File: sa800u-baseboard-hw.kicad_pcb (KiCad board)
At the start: 2 copper layers, 100 x 70 mm, 171 parts, among them IC1 TPS2378DDA, J1 WE-RJ45_7499111121A, J10 2908-05WB-MG, J11 MC-HVT1-S04-G, J12 MC-HVT1-S04-G, J13 MC-HVT1-S04-G, J14 MC-HVT1-S04-G, J2 46756-1001, J4 WE_632723300011, J5 WE_632723300011, J6 WE_632723300011, J7 3-84952-0, J8 F52R-1A7H1-11020, J9 WE_68715014522, Q1 2N7000, Q2 2N7000, Q3 2N7000, T1 749020010A, U1 RTL8111H, U10 MDT580M01001, U11 AP62301Z6-7, U12 AP62301Z6-7, U13 TPS65982BB, U2 LT9611, U3 TXB0104RUT, U4 TXS0102YZPR, U5 TS3USB30EDGSR, U6 FT2232HL-REEL, U7 USB57442G, U8 SA800U-WF, U9 MAX13042EEBC+T, Y1 ECS-1618-250-BN-TR, Y2 ECS-1618-250-BN-TR

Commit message: Import changes to PCB, group components
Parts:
- removed the C7 at (111.8, 27.7)
- removed the C8 at (143.0, 9.42)
- removed J11, J12, J13, J14: MC-HVT1-S04-G, sa800u-baseboard-hw-footprints:PinHeader_1x4_P1.27mm_Drill.7mm
- removed the J5 at (113.0, 147.5)
- removed the J6 at (125.5, 147.5)
- removed the R17 at (124.2, 24.5)
- removed the R36 at (58.4, 54.8)
- removed T1: 749020010A, sa800u-baseboard-hw-footprints:749020010A
- removed the U10 at (69.0, 143.0)
- removed the U11 at (137.3, -17.1)
- added C107: C_100u_0805, sa800u-baseboard-hw-footprints:0805-cap, F.Cu at (135.0, 123.3)
- added C108: C_100u_0805, sa800u-baseboard-hw-footprints:0805-cap, F.Cu at (135.0, 125.3)
- added C109: C_10u_25V_0603, antmicro-footprints:0603-cap, F.Cu at (225.6, 78.6)
- added C11: C_22u_0603, antmicro-footprints:0603-cap, F.Cu at (256.2, 71.7)
- added C110: C_100n_0402, antmicro-footprints:0402-cap, F.Cu at (220.3, 75.5)
- added C111: C_22u_0603, antmicro-footprints:0603-cap, F.Cu at (225.6, 81.3)
- added C112: C_22u_0603, antmicro-footprints:0603-cap, F.Cu at (227.1, 81.3)
- added C113: C_100n_0402, sa800u-baseboard-hw-footprints:0402-cap, F.Cu at (265.4, 68.4)
- added C114: C_22u_0603, antmicro-footprints:0603-cap, F.Cu at (243.0, 73.1)
- added C115: C_22u_0603, antmicro-footprints:0603-cap, F.Cu at (256.2, 74.4)
- added C116: C_22u_0603, antmicro-footprints:0603-cap, F.Cu at (272.2, 74.2)
- added C117: C_22u_0603, antmicro-footprints:0603-cap, F.Cu at (241.5, 73.1)
- added C118: C_22u_0603, antmicro-footprints:0603-cap, F.Cu at (257.7, 74.4)
- added C119: C_22u_0603, antmicro-footprints:0603-cap, F.Cu at (270.7, 74.2)
- added C14: C_100n_0402, sa800u-baseboard-hw-footprints:0402-cap, F.Cu at (236.2, 67.3)
- added C15: C_100n_0402, sa800u-baseboard-hw-footprints:0402-cap, F.Cu at (96.1, -22.1)
- added C16: C_100n_0402, sa800u-baseboard-hw-footprints:0402-cap, F.Cu at (250.9, 68.6)
- added C17: C_100n_0402, sa800u-baseboard-hw-footprints:0402-cap, F.Cu at (95.6, -16.2)
- added C18: C_100n_0402, sa800u-baseboard-hw-footprints:0402-cap, F.Cu at (105.1, -22.1)
- added C2: C_100n_0402, sa800u-baseboard-hw-footprints:0402-cap, F.Cu at (96.1, -19.9)
- added C20: C_10p_0402, sa800u-baseboard-hw-footprints:0402-cap, F.Cu at (101.6, -24.7)
- added C21: C_10p_0402, sa800u-baseboard-hw-footprints:0402-cap, F.Cu at (97.0, -24.6)
- added C22: C_10u_0402, sa800u-baseboard-hw-footprints:0402-cap, F.Cu at (90.8, 21.0)
- added C23: C_1u_0402, sa800u-baseboard-hw-footprints:0402-cap, F.Cu at (90.8, 22.0)
- added C24: C_100n_0402, sa800u-baseboard-hw-footprints:0402-cap, F.Cu at (90.8, 23.0)
- added C25: C_100n_0402, sa800u-baseboard-hw-footprints:0402-cap, F.Cu at (90.8, 24.0)
- added C26: C_10u_0402, sa800u-baseboard-hw-footprints:0402-cap, F.Cu at (87.1, 21.0)
- added C27: C_100n_0402, sa800u-baseboard-hw-footprints:0402-cap, F.Cu at (87.1, 22.0)
- added C29: C_100n_0402, sa800u-baseboard-hw-footprints:0402-cap, F.Cu at (87.1, 23.0)
- added C3: C_100n_0402, sa800u-baseboard-hw-footprints:0402-cap, F.Cu at (98.7, -13.9)
- added C30: C_100n_0402, sa800u-baseboard-hw-footprints:0402-cap, F.Cu at (87.1, 24.0)
- added C31: C_10u_0402, sa800u-baseboard-hw-footprints:0402-cap, F.Cu at (84.1, 21.0)
- added C32: C_100n_0402, sa800u-baseboard-hw-footprints:0402-cap, F.Cu at (84.1, 22.0)
- added C33: C_10u_0402, sa800u-baseboard-hw-footprints:0402-cap, F.Cu at (80.8, 21.0)
- added C34: C_1u_0402, sa800u-baseboard-hw-footprints:0402-cap, F.Cu at (80.8, 22.0)
- added C35: C_100n_0402, sa800u-baseboard-hw-footprints:0402-cap, F.Cu at (80.8, 23.0)
- added C36: C_100n_0402, sa800u-baseboard-hw-footprints:0402-cap, F.Cu at (80.8, 24.0)
- added C37: C_100n_0402, sa800u-baseboard-hw-footprints:0402-cap, F.Cu at (80.8, 25.0)
- added C38: C_100n_0402, sa800u-baseboard-hw-footprints:0402-cap, F.Cu at (80.8, 26.0)
- added C39: C_10u_0402, sa800u-baseboard-hw-footprints:0402-cap, F.Cu at (78.1, 21.0)
- added C40: C_100n_0402, sa800u-baseboard-hw-footprints:0402-cap, F.Cu at (78.1, 22.0)
- added C41: C_100n_0402, sa800u-baseboard-hw-footprints:0402-cap, F.Cu at (78.1, 23.0)
- added C43: C_15p_0402, sa800u-baseboard-hw-footprints:0402-cap, F.Cu at (111.3, 11.9)
- added C44: C_10u_0402, sa800u-baseboard-hw-footprints:0402-cap, F.Cu at (75.3, 21.0)
- added C45: C_100n_0402, sa800u-baseboard-hw-footprints:0402-cap, F.Cu at (75.3, 22.0)
- added C47: C_15p_0402, sa800u-baseboard-hw-footprints:0402-cap, F.Cu at (106.8, 11.9)
- added C49: C_100n_0402, sa800u-baseboard-hw-footprints:0402-cap, F.Cu at (39.3, 69.0)
- added C50: C_100n_0402, sa800u-baseboard-hw-footprints:0402-cap, F.Cu at (38.3, 69.0)
- added C51: C_100n_0402, sa800u-baseboard-hw-footprints:0402-cap, F.Cu at (35.8, 69.0)
- added C52: C_100n_0402, sa800u-baseboard-hw-footprints:0402-cap, F.Cu at (34.8, 69.0)
- added C53: C_100n_0402, sa800u-baseboard-hw-footprints:0402-cap, F.Cu at (32.2, 69.0)
- added C54: C_100n_0402, sa800u-baseboard-hw-footprints:0402-cap, F.Cu at (31.2, 69.0)
- added C55: C_100n_0402, sa800u-baseboard-hw-footprints:0402-cap, F.Cu at (28.5, 69.0)
- added C56: C_100n_0402, sa800u-baseboard-hw-footprints:0402-cap, F.Cu at (27.5, 69.0)
- added C57: C_100n_0402, sa800u-baseboard-hw-footprints:0402-cap, F.Cu at (27.6, 77.9)
- added C58: C_10p_0402, sa800u-baseboard-hw-footprints:0402-cap, F.Cu at (29.5, 69.0)
- added C59: C_10p_0402, sa800u-baseboard-hw-footprints:0402-cap, F.Cu at (26.5, 69.0)
- added C60: C_47u_0603, sa800u-baseboard-hw-footprints:0603-cap, F.Cu at (158.5, 47.4)
- added C61: C_47u_0603, sa800u-baseboard-hw-footprints:0603-cap, F.Cu at (158.5, 45.9)
- added C62: C_47u_0603, sa800u-baseboard-hw-footprints:0603-cap, F.Cu at (161.1, 45.9)
- added C63: C_47u_0603, sa800u-baseboard-hw-footprints:0603-cap, F.Cu at (158.5, 44.4)
- added C66: C_330n_0603, sa800u-baseboard-hw-footprints:0603-res, F.Cu at (99.3, 138.7)
- added C69: C_100n_0402, sa800u-baseboard-hw-footprints:0402-cap, F.Cu at (157.3, 53.1)
- added C70: C_100n_0402, sa800u-baseboard-hw-footprints:0402-cap, F.Cu at (157.3, 56.7)
- added C71: C_22u_0603, sa800u-baseboard-hw-footprints:0603-cap, F.Cu at (163.8, 54.2)
- added C72: C_100n_0402, sa800u-baseboard-hw-footprints:0402-cap, F.Cu at (157.3, 52.1)
- added C73: C_100n_0402, sa800u-baseboard-hw-footprints:0402-cap, F.Cu at (157.3, 55.7)
- added C74: C_100n_0402, sa800u-baseboard-hw-footprints:0402-cap, F.Cu at (163.5, 52.9)
- added C75: C_10u_0402, sa800u-baseboard-hw-footprints:0402-cap, F.Cu at (163.8, 46.3)
- added C80: C_100n_0402, sa800u-baseboard-hw-footprints:0402-cap, F.Cu at (154.6, 52.1)
- added C81: C_100n_0402, sa800u-baseboard-hw-footprints:0402-cap, F.Cu at (154.7, 56.7)
- added C82: C_100n_0402, sa800u-baseboard-hw-footprints:0402-cap, F.Cu at (154.6, 53.1)
- added C83: C_100n_0402, sa800u-baseboard-hw-footprints:0402-cap, F.Cu at (154.7, 55.7)
- added C85: C_100n_0402, sa800u-baseboard-hw-footprints:0402-cap, F.Cu at (171.8, 43.0)
- added C86: C_100n_0402, sa800u-baseboard-hw-footprints:0402-cap, F.Cu at (174.9, 46.4)
- added C87: C_100n_0402, sa800u-baseboard-hw-footprints:0402-cap, F.Cu at (174.9, 39.6)
- added C88: C_100n_0402, sa800u-baseboard-hw-footprints:0402-cap, F.Cu at (147.0, 57.0)
- added C89: C_100n_0402, sa800u-baseboard-hw-footprints:0402-cap, F.Cu at (141.4, 57.0)
- added C92: C_100u_0805, sa800u-baseboard-hw-footprints:0805-cap, F.Cu at (135.0, 127.3)
- added C93: C_100n_0402, sa800u-baseboard-hw-footprints:0402-cap, F.Cu at (137.9, 124.9)
- added C94: C_33p_0402, sa800u-baseboard-hw-footprints:0402-cap, F.Cu at (137.9, 125.9)
- added C95: C_10p_0402, sa800u-baseboard-hw-footprints:0402-cap, F.Cu at (137.9, 126.9)
- added C96: C_1u_0402, sa800u-baseboard-hw-footprints:0402-cap, F.Cu at (178.1, -9.90)
- added C97: C_100n_0402, sa800u-baseboard-hw-footprints:0402-cap, F.Cu at (183.0, -9.50)
- added C98: C_100n_0402, sa800u-baseboard-hw-footprints:0402-cap, F.Cu at (181.0, -11.1)
- added D10: ESD9L5.0ST5G, sa800u-baseboard-hw-footprints:DIOM1006X40N, F.Cu at (87.7, 135.9)
- added D12: ESD9L5.0ST5G, sa800u-baseboard-hw-footprints:DIOM1006X40N, F.Cu at (163.9, 51.8)
- added D13: TPD1E10B06DPYR, sa800u-baseboard-hw-footprints:XDFN-2_1x0.60mm, F.Cu at (91.2, 137.0)
- added D14: RCLAMP2504N.TCT, sa800u-baseboard-hw-footprints:RCLAMP2504N.TCT, F.Cu at (145.0, 98.9)
- added D15: STS321045B502, sa800u-baseboard-hw-footprints:STS321045B502, F.Cu at (139.0, 123.4)
- added D19: BZT52C12, sa800u-baseboard-hw-footprints:SOD-123, B.Cu at (28.7, -18.1)
- added D8: ESD9L5.0ST5G, sa800u-baseboard-hw-footprints:DIOM1006X40N, F.Cu at (167.4, 55.5)
- added D9: ESD9L5.0ST5G, sa800u-baseboard-hw-footprints:DIOM1006X40N, F.Cu at (87.7, 134.7)
- added J10: 1053091202, sa800u-baseboard-hw-footprints:1053091202, F.Cu at (216.7, 62.8)
- added J4: WE_632723300011, sa800u-baseboard-hw-footprints:WE_632723300011, F.Cu at (161.9, 62.1)
- added J7: MC-HVT1-S04-G, sa800u-baseboard-hw-footprints:PinHeader_1x4_P1.27mm_Drill.7mm, F.Cu at (109.5, 60.0)
- added L1: BRC1608TR35M, sa800u-baseboard-hw-footprints:INDC1608X100N, F.Cu at (91.3, 26.1)
- added L10: NFP0QHB242HS2D, sa800u-baseboard-hw-footprints:FIL_NFP0QHB242HS2D, B.Cu at (138.2, 146.5)
- added L19: NFP0QHB242HS2D, sa800u-baseboard-hw-footprints:FIL_NFP0QHB242HS2D, B.Cu at (102.0, 88.0)
- added L2: BRC1608TR35M, sa800u-baseboard-hw-footprints:INDC1608X100N, F.Cu at (87.6, 26.1)
- added L29: XEL4030-222MEC, antmicro-footprints:Coilcraft-XEL4030, F.Cu at (222.7, 80.8)
- added L3: BRC1608TR35M, sa800u-baseboard-hw-footprints:INDC1608X100N, F.Cu at (84.6, 24.1)
- added L30: XEL4030-222MEC, antmicro-footprints:Coilcraft-XEL4030, F.Cu at (238.6, 72.6)
- added L31: XEL4030-222MEC, antmicro-footprints:Coilcraft-XEL4030, F.Cu at (253.3, 73.9)
- added L32: XEL4030-222MEC, antmicro-footprints:Coilcraft-XEL4030, F.Cu at (267.8, 73.7)
- added L4: BRC1608TR35M, sa800u-baseboard-hw-footprints:INDC1608X100N, F.Cu at (81.3, 28.1)
- added L5: BRC1608TR35M, sa800u-baseboard-hw-footprints:INDC1608X100N, F.Cu at (78.6, 25.1)
- added L6: BRC1608TR35M, sa800u-baseboard-hw-footprints:INDC1608X100N, F.Cu at (75.9, 24.1)
- added L7: NFP0QHB242HS2D, sa800u-baseboard-hw-footprints:FIL_NFP0QHB242HS2D, F.Cu at (139.9, 142.1)
- added L8: NFP0QHB242HS2D, sa800u-baseboard-hw-footprints:FIL_NFP0QHB242HS2D, B.Cu at (139.4, 146.5)
- added Q4: 2N7000, sa800u-baseboard-hw-footprints:TO-92-3, F.Cu at (25.3, 75.2)
- added Q5: BSS84PH6327XTSA2, sa800u-baseboard-hw-footprints:SOT-23-3, F.Cu at (220.6, 70.6)
- added Q6: IRF7416TRPBF, antmicro-footprints:IRF7416TRPBF, F.Cu at (224.1, 64.5)
- added R10: R_10k_0402, antmicro-footprints:0402-res, F.Cu at (269.9, 66.5)
- added R15: R_1M0_0402, sa800u-baseboard-hw-footprints:0402-res, F.Cu at (99.2, -20.9)
- added R39: R_50R_0402, sa800u-baseboard-hw-footprints:0402-res, F.Cu at (27.5, 67.0)
- added R40: R_1M0_0402, sa800u-baseboard-hw-footprints:0402-res, F.Cu at (109.1, 15.7)
- added R41: R_50R_0402, sa800u-baseboard-hw-footprints:0402-res, F.Cu at (28.5, 67.0)
- added R42: R_50R_0402, sa800u-baseboard-hw-footprints:0402-res, F.Cu at (31.2, 67.0)
- added R43: R_50R_0402, sa800u-baseboard-hw-footprints:0402-res, F.Cu at (32.2, 67.0)
- added R44: R_50R_0402, sa800u-baseboard-hw-footprints:0402-res, F.Cu at (34.8, 67.0)
- added R45: R_50R_0402, sa800u-baseboard-hw-footprints:0402-res, F.Cu at (35.8, 67.0)
- added R46: R_50R_0402, sa800u-baseboard-hw-footprints:0402-res, F.Cu at (38.3, 67.0)
- added R51: R_50R_0402, sa800u-baseboard-hw-footprints:0402-res, F.Cu at (39.3, 67.0)
- added R52: R_510R_0603, sa800u-baseboard-hw-footprints:0603-res, F.Cu at (39.5, 71.3)
- added R53: R_10k_0402, sa800u-baseboard-hw-footprints:0402-res, F.Cu at (136.2, 141.8)
- added R54: R_510R_0603, sa800u-baseboard-hw-footprints:0603-res, F.Cu at (38.0, 71.3)
- added R55: R_20k_0402, sa800u-baseboard-hw-footprints:0402-res, F.Cu at (141.1, 141.8)
- added R56: R_510R_0603, sa800u-baseboard-hw-footprints:0603-res, F.Cu at (36.0, 71.3)
- added R57: R_510R_0603, sa800u-baseboard-hw-footprints:0603-res, F.Cu at (34.5, 71.3)
- added R58: R_510R_0603, sa800u-baseboard-hw-footprints:0603-res, F.Cu at (32.5, 71.3)
- added R59: R_10k_0402, sa800u-baseboard-hw-footprints:0402-res, F.Cu at (26.6, 77.9)
- added R60: R_510R_0603, sa800u-baseboard-hw-footprints:0603-res, F.Cu at (30.9, 71.3)
- added R61: R_510R_0603, sa800u-baseboard-hw-footprints:0603-res, F.Cu at (28.8, 71.3)
- added R62: R_510R_0603, sa800u-baseboard-hw-footprints:0603-res, F.Cu at (27.2, 71.3)
- added R63: R_100k_0.5%_0402, sa800u-baseboard-hw-footprints:0402, F.Cu at (164.3, 49.0)
- added R64: R_100k_0402, sa800u-baseboard-hw-footprints:0402-res, F.Cu at (164.3, 50.1)
- added R65: R_100k_0402, sa800u-baseboard-hw-footprints:0402-res, F.Cu at (159.4, 50.1)
- added R66: R_100k_0402, sa800u-baseboard-hw-footprints:0402-res, F.Cu at (159.4, 49.1)
- added R67: R_200k_0402, sa800u-baseboard-hw-footprints:0402-res, F.Cu at (172.3, 45.4)
- added R73: R_1k_0402, sa800u-baseboard-hw-footprints:0402-res, F.Cu at (147.4, 100.6)
- added R74: R_1k_0402, sa800u-baseboard-hw-footprints:0402-res, F.Cu at (147.4, 92.5)
- added R75: R_1k_0402, sa800u-baseboard-hw-footprints:0402-res, F.Cu at (147.4, 96.6)
- added R76: R_1k_0402, sa800u-baseboard-hw-footprints:0402-res, F.Cu at (147.4, 104.6)
- added R87: R_7k5_2512, sa800u-baseboard-hw-footprints:2512-res, F.Cu at (21.9, -20.4)
- added R91: R_7k5_0402, antmicro-footprints:0402-res, F.Cu at (217.0, 69.7)
- added R92: R_2k2_0402, antmicro-footprints:0402-res, F.Cu at (215.5, 70.2)
- added R93: R_2k2_0402, antmicro-footprints:0402-res, F.Cu at (218.1, 69.7)
- added R94: R_1k_0402, sa800u-baseboard-hw-footprints:0402-res, F.Cu at (219.6, 73.0)
- added R95: R_25k5_0402, sa800u-baseboard-hw-footprints:0402-res, F.Cu at (221.7, 73.5)
- added R96: R_10k_0402, sa800u-baseboard-hw-footprints:0402-res, F.Cu at (222.7, 73.5)
- added R97: R_52k3_0402, antmicro-footprints:0402-res, F.Cu at (224.7, 73.5)
- added R98: R_10k_0402, antmicro-footprints:0402-res, F.Cu at (223.7, 73.5)
- added R99: R_20k_0402, antmicro-footprints:0402-res, F.Cu at (268.9, 66.5)
- added U14: AP62301WU-7, sa800u-baseboard-hw-footprints:TSOT23-6, F.Cu at (253.3, 69.7)
- added U15: AP62301WU-7, sa800u-baseboard-hw-footprints:TSOT23-6, F.Cu at (267.8, 69.5)
- added U16: LMV431IM5, antmicro-footprints:SOT-23-5, F.Cu at (216.4, 72.6)
- added U17: AP62301WU-7, sa800u-baseboard-hw-footprints:TSOT23-6, F.Cu at (222.7, 76.6)
- added U5: TPS25820DSST, sa800u-baseboard-hw-footprints:WSON-12_2x3mm, F.Cu at (161.8, 48.3)
- added U8: CBTL02043ABQ,115, sa800u-baseboard-hw-footprints:DHVQFN20, F.Cu at (174.9, 43.0)
- C1: value C_1n_1210_2kV -> C_10n_0402; footprint sa800u-baseboard-hw-footprints:1210-cap -> antmicro-footprints:0402-cap
- C10, C12: value C_10p_0402 -> C_100n_0402
- C100: renamed from C30; moved to B.Cu
- C101: renamed from C31; moved to B.Cu
- C102: renamed from C32; moved to B.Cu
- C103: renamed from C33; moved to B.Cu
- C104: renamed from C34; moved to B.Cu
- C105: renamed from C35; moved to B.Cu
- C13, C9: value C_10p_0402 -> C_22u_0603; footprint sa800u-baseboard-hw-footprints:0402-cap -> antmicro-footprints:0603-cap
- C19: value C_330n_0603 -> C_1u_0402; footprint sa800u-baseboard-hw-footprints:0603-res -> sa800u-baseboard-hw-footprints:0402-cap
- C4, C5: value C_10n_0402 -> C_4u7_0402
- C6: value C_1n_1210_2kV -> C_100n_0402; footprint sa800u-baseboard-hw-footprints:1210-cap -> sa800u-baseboard-hw-footprints:0402-cap
- C99: renamed from C29; moved to B.Cu
- D1, D2: value BZX84C6V2LT1G -> BZX84C3V3LT1G; footprint sa800u-baseboard-hw-footprints:SOT-23-3 -> antmicro-footprints:SOT-23-3
- D11: value BZT52Bxx -> TPD1E10B06DPYR; footprint sa800u-baseboard-hw-footprints:SOD-123 -> sa800u-baseboard-hw-footprints:XDFN-2_1x0.60mm
- D18: renamed from D10; moved to B.Cu
- D4, D5: value BZX84-C3V6,215 -> TPD1E10B06DPYR; footprint sa800u-baseboard-hw-footprints:SOT95P230X110-3N -> sa800u-baseboard-hw-footprints:XDFN-2_1x0.60mm
- D6: value PGB1010603MR -> TPD1E10B06DPYR; footprint sa800u-baseboard-hw-footprints:PGB1010603MR -> sa800u-baseboard-hw-footprints:XDFN-2_1x0.60mm
- D7: value PGB1010603MR -> ESD9L5.0ST5G; footprint sa800u-baseboard-hw-footprints:PGB1010603MR -> sa800u-baseboard-hw-footprints:DIOM1006X40N
- J1: value WE-RJ45_7499111121A -> 5-2337992-8; footprint sa800u-baseboard-hw-footprints:7499111121A -> antmicro-footprints:5-2337992-8
- L11: renamed from L1; moved to B.Cu
- L12: renamed from L2; moved to B.Cu
- L13: renamed from L3; moved to B.Cu
- L20: renamed from L10; moved to B.Cu
- L21: renamed from L11; moved to B.Cu
- L22: renamed from L12; moved to B.Cu
- L23: renamed from L13; moved to B.Cu
- L24: renamed from L14; moved to B.Cu
- L25: renamed from L15; moved to B.Cu
- L26: renamed from L16; moved to B.Cu
- L27: renamed from L17; moved to B.Cu
- L28: renamed from L18; moved to B.Cu
- MP1, MP2, MP3, MP4: value PCB_Mount_Hole_3_NPTH -> PCB_Spacer_M2; footprint sa800u-baseboard-hw-footprints:mounting-hole-3mm-NPTH -> antmicro-footprints:9774030243R; moved to B.Cu
- R1, R2, R3, R7: value R_75R_0402 -> R_10k_0402; footprint sa800u-baseboard-hw-footprints:0402-res -> antmicro-footprints:0402-res
- R4: value R_75R_0402 -> R_31k6_0402; footprint sa800u-baseboard-hw-footprints:0402-res -> antmicro-footprints:0402-res
- R6: value R_75R_0402 -> R_0R_0402
- R8: value R_75R_0402 -> R_25k_1%_0402; footprint sa800u-baseboard-hw-footprints:0402-res -> antmicro-footprints:0402
- R85: renamed from R52; moved to B.Cu
- R86: renamed from R53; moved to B.Cu
- R88: renamed from R54; moved to B.Cu
- R89: renamed from R55; moved to B.Cu
- R9: value R_75R_0402 -> R_20k_0402; footprint sa800u-baseboard-hw-footprints:0402-res -> antmicro-footprints:0402-res
- R90: renamed from R56; moved to B.Cu
- U12: value AP62301Z6-7 -> MDT580M01001; footprint sa800u-baseboard-hw-footprints:SOT-563 -> sa800u-baseboard-hw-footprints:MDT580M01001; moved to B.Cu
- U13: value TPS65982BB -> AP62301WU-7; footprint sa800u-baseboard-hw-footprints:TPS65982ABZBHR -> sa800u-baseboard-hw-footprints:TSOT23-6; moved to F.Cu
- U2: footprint sa800u-baseboard-hw-footprints:LT9611 -> antmicro-footprints:LT9611
- U7: value USB57442G -> TXB0104D; footprint sa800u-baseboard-hw-footprints:QFN40P700X700X100-57N -> sa800u-baseboard-hw-footprints:SOIC-14_W3.9mm
- Y1: value ECS-1618-250-BN-TR -> ABM8G-25.000MHZ-18-D2Y-T; footprint sa800u-baseboard-hw-footprints:OSC_ECS-1618-250-BN-TR -> sa800u-baseboard-hw-footprints:KX-7
- Y2: value ECS-1618-250-BN-TR -> ABM8G-24.000MHZ-18-D2Y-T; footprint sa800u-baseboard-hw-footprints:OSC_ECS-1618-250-BN-TR -> sa800u-baseboard-hw-footprints:KX-7
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- renumbered C36 to C106, C11 to C28, C14 to C42, C15 to C46, C16 to C48, C17 to C64, C18 to C65, C20 to C67, C21 to C68, C2 to C7, C22 to C76, C23 to C77, C24 to C78, C25 to C79, C3 to C8, C26 to C84, C27 to C90, C28 to C91, D8 to D16, D9 to D17, J4 to J3, J7 to J5, J8 to J6, J9 to J8, J10 to J9, L4 to L14, L5 to L15, L6 to L16, L7 to L17, L8 to L18, R10 to R11, R11 to R12, R12 to R13, R13 to R14, R14 to R16, R15 to R17, R16 to R18, R18 to R19, R19 to R20, R24 to R21, R20 to R22, R21 to R23, R22 to R24, R23 to R25, R28 to R26, R29 to R27, R25 to R28, R34 to R29, R35 to R30, R30 to R31, R31 to R32, R32 to R33, R33 to R34, R26 to R35, R27 to R36, R41 to R47, R42 to R48, R39 to R49, R40 to R50, R43 to R68, R44 to R69, R45 to R70, R46 to R71, R47 to R72, R57 to R77, R58 to R78, R59 to R79, R60 to R80, R61 to R81, R62 to R82, R50 to R83, R51 to R84, S4 to S1, S1 to S2, S2 to S3, S3 to S4, U8 to U10, U9 to U11, U5 to U6, U6 to U9
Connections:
- net /PoE/VDD renamed /PoE/VDD_POE
- net ETH_ISOLATEB renamed /Ethernet_Controller/ETH_ISOLATEB
- net I2C_ADDR renamed /HDMI_converter/I2C_ADDR
- net PCIE1_CLKREQ_N renamed /Ethernet_Controller/PCIE1_CLKREQ_N
- net PCIE1_RST_N renamed /Ethernet_Controller/PCIE1_RST_N
- net PCIE1_WAKE_N renamed /Ethernet_Controller/PCIE1_WAKE_N
- BAT1 pad +: Net-(BAT1-Pad+) -> VRTC
- BAT1 pad -: Net-(BAT1-Pad-) -> GND
- C1 pad 1: GND -> Net-(C1-Pad1)
- C1 pad 2: Net-(C1-Pad2) -> Earth
- C10 pad 1: /Ethernet_Controller/XTAL2 -> /Ethernet_Controller/ETH_1V0
- C102 pad 1: 5V -> VDD
- C103 pad 1: 5V -> VDD
- C104 pad 1: 5V -> VDD
- C105 pad 1: 5V -> VDD
- C106 pad 2: Net-(C36-Pad2) -> GNDD
- C12 pad 1: /HDMI_converter/XTALO -> /Ethernet_Controller/ETH_1V0
- C13 pad 1: /HDMI_converter/XTALI -> 5V
- C19 pad 1: VBUS -> /Ethernet_Controller/ETH_1V0
- C19 pad 2: /USB-C_Interface /USB1_SS_RX1_N -> GND
- C4 pad 1: PAIR78 -> 3V3
- C4 pad 2: Net-(C4-Pad2) -> GND
- C5 pad 1: PAIR45 -> 3V3
- C5 pad 2: Net-(C5-Pad2) -> GND
- C6 pad 1: Earth -> /Ethernet_Controller/REG_1V0
- C6 pad 2: Net-(C6-Pad2) -> GND
- C64 pad 2: /USB-C_Interface /USB1_SS_TX0_P -> USB1_SS_TX0_P
- C65 pad 2: /USB-C_Interface /USB1_SS_TX0_N -> USB1_SS_TX0_N
- C67 pad 2: /USB-C_Interface /USB1_SS_RX1_P -> USB1_SS_RX1_P
- C68 pad 1: VBUS -> USB_VBUS
- C76 pad 1: /USB-C_Interface /USB1_SS_RX0_P -> USB1_SS_RX0_P
- C77 pad 1: /USB-C_Interface /USB1_SS_RX0_N -> USB1_SS_RX0_N
- C78 pad 1: /USB-C_Interface /USB1_SS_TX1_N -> USB1_SS_TX1_N
- C79 pad 1: /USB-C_Interface /USB1_SS_TX1_P -> USB1_SS_TX1_P
- C9 pad 1: /Ethernet_Controller/XTAL1 -> 5V
- D1 pad 1: GND -> (no net)
- D1 pad 3: /Ethernet_Controller/ETH_LED0 -> (no net)
- D2 pad 1: GND -> (no net)
- D2 pad 3: /Ethernet_Controller/ETH_LED2 -> (no net)
- D4 pad 1: GND -> /HDMI_converter/SCL_HDMI
- D4 pad 2: (no net) -> GND
- D5 pad 1: GND -> /HDMI_converter/SDA_HDMI
- D5 pad 2: (no net) -> GND
- D6 pad 1: /USB-C_Interface /USB_CC1 -> /HDMI_converter/DETECT_HDMI
- IC1 pad 5: Net-(C36-Pad2) -> GNDD
- IC1 pad 7: T2P_HIGH -> (no net)
- IC1 pad 8: APD -> (no net)
- J1 pad 1: /Ethernet_Controller/LAN0_RJ45_D1_P -> /Ethernet_Controller/LAN0_MDI0_N
- J1 pad 10: Earth -> /Ethernet_Controller/LAN0_MDI3_P
- J1 pad 11: Net-(J1-Pad11) -> PAIR12
- J1 pad 12: /Ethernet_Controller/ETH_LED0 -> PAIR36
- J1 pad 13: Net-(J1-Pad13) -> PAIR45
- J1 pad 14: /Ethernet_Controller/ETH_LED2 -> PAIR78
- J1 pad 2: /Ethernet_Controller/LAN0_RJ45_D1_N -> /Ethernet_Controller/LAN0_MDI0_P
- J1 pad 3: /Ethernet_Controller/LAN0_RJ45_D2_P -> /Ethernet_Controller/LAN0_MDI1_N
- J1 pad 4: /Ethernet_Controller/LAN0_RJ45_D3_P -> Net-(C1-Pad1)
- J1 pad 5: /Ethernet_Controller/LAN0_RJ45_D3_N -> Net-(C1-Pad1)
- J1 pad 6: /Ethernet_Controller/LAN0_RJ45_D2_N -> /Ethernet_Controller/LAN0_MDI1_P
- J1 pad 7: /Ethernet_Controller/LAN0_RJ45_D4_P -> /Ethernet_Controller/LAN0_MDI2_N
- J1 pad 8: /Ethernet_Controller/LAN0_RJ45_D4_N -> /Ethernet_Controller/LAN0_MDI2_P
- J1 pad 9: 3V3 -> /Ethernet_Controller/LAN0_MDI3_N
- J2 pad 1: Net-(J2-Pad1) -> /HDMI_converter/DETECT_HDMI
- J2 pad 10: Net-(J2-Pad10) -> GND
- J2 pad 13: Net-(J2-Pad13) -> GND
- J2 pad 15: Net-(J2-Pad15) -> /HDMI_converter/CEC_HDMI
- J2 pad 16: Net-(J2-Pad16) -> GND
- J2 pad 17: Net-(J2-Pad17) -> /HDMI_converter/SCL_HDMI
- J2 pad 18: Net-(J2-Pad18) -> /HDMI_converter/SDA_HDMI
- J2 pad 19: Net-(J2-Pad19) -> 5V
- J2 pad 2: Net-(J2-Pad2) -> (no net)
- J2 pad 4: Net-(J2-Pad4) -> GND
- J2 pad 7: Net-(J2-Pad7) -> GND
- J2 pad SH: Net-(J2-PadSH) -> GND
- J3 pad A10: VBUS -> USB_VBUS
- J3 pad A4: VBUS -> USB_VBUS
- J3 pad A6: /USB-C_Interface /USB1_DP -> USB1_DP
- J3 pad A7: /USB-C_Interface /USB1_DM -> USB1_DM
- J3 pad A9: VBUS -> USB_VBUS
- J3 pad B4: VBUS -> USB_VBUS
- J3 pad B6: /USB-C_Interface /USB1_DP -> USB1_DP
- J3 pad B7: /USB-C_Interface /USB1_DM -> USB1_DM
- J3 pad B9: VBUS -> USB_VBUS
- J3 pad Shell: Net-(J4-PadShell) -> GND
- J5 pad 11: /LCM/TP_I2C_SCL -> TP_I2C_SCL
- J5 pad 12: /LCM/TP_I2C_SDA -> TP_I2C_SDA
- J5 pad 14: +3V3 -> 3V3
- J5 pad 15: +3V3 -> 3V3
- J5 pad 16: Net-(J7-Pad16) -> (no net)
- J5 pad 17: Net-(J7-Pad17) -> (no net)
- J5 pad 18: Net-(J7-Pad18) -> (no net)
- J5 pad 19: Net-(J7-Pad19) -> (no net)
- J5 pad 20: Net-(J7-Pad20) -> (no net)
- J5 pad 21: Net-(J7-Pad21) -> (no net)
- J5 pad 22: Net-(J7-Pad22) -> (no net)
- J5 pad 23: Net-(J7-Pad23) -> (no net)
- J5 pad 24: Net-(J7-Pad24) -> (no net)
- J5 pad 25: Net-(J7-Pad25) -> (no net)
- J5 pad 26: Net-(J7-Pad26) -> (no net)
- J5 pad 27: Net-(J7-Pad27) -> (no net)
- J5 pad 28: Net-(J7-Pad28) -> (no net)
- J5 pad 29: Net-(J7-Pad29) -> (no net)
- J5 pad 30: Net-(J7-Pad30) -> (no net)
- J6 pad 17: /LCM/TP_I2C_SCL -> TP_I2C_SCL
- J6 pad 18: /LCM/TP_I2C_SDA -> TP_I2C_SDA
- J6 pad 20: +3V3 -> 3V3
- J8 pad 13: Net-(J9-Pad13) -> (no net)
- J8 pad 14: Net-(J9-Pad14) -> (no net)
- J8 pad 16: Net-(J9-Pad16) -> (no net)
- J8 pad 17: Net-(J9-Pad17) -> (no net)
- J8 pad 31: Net-(J9-Pad31) -> (no net)
- J8 pad 35: Net-(J9-Pad35) -> (no net)
- J8 pad 36: Net-(J9-Pad36) -> (no net)
- J8 pad 37: Net-(J9-Pad37) -> (no net)
- J8 pad 38: Net-(J9-Pad38) -> (no net)
- J8 pad 43: Net-(J9-Pad43) -> (no net)
- J8 pad 44: Net-(J9-Pad44) -> (no net)
- J8 pad 45: Net-(J9-Pad45) -> (no net)
- J8 pad 46: Net-(J9-Pad46) -> (no net)
- J9 pad 1: Net-(J10-Pad1) -> (no net)
- J9 pad 2: Net-(J10-Pad2) -> (no net)
- J9 pad 3: Net-(J10-Pad3) -> (no net)
- J9 pad 4: Net-(J10-Pad4) -> (no net)
- J9 pad 5: Net-(J10-Pad5) -> (no net)
- J9 pad 6: Net-(J10-Pad6) -> (no net)
- J9 pad 7: Net-(J10-Pad7) -> (no net)
- J9 pad 8: Net-(J10-Pad8) -> (no net)
- L11 pad 1: /LCM/DSI0_LN1_N -> DSI0_LN1_N
- L11 pad 4: /LCM/DSI0_LN1_P -> DSI0_LN1_P
- L12 pad 1: /LCM/DSI0_CLK_N -> DSI0_CLK_N
- L12 pad 4: /LCM/DSI0_CLK_P -> DSI0_CLK_P
- L13 pad 1: /LCM/DSI0_LN0_N -> DSI0_LN0_N
- L13 pad 4: /LCM/DSI0_LN0_P -> DSI0_LN0_P
- L14 pad 1: /LCM/DSI0_LN3_N -> DSI0_LN3_N
- L14 pad 4: /LCM/DSI0_LN3_P -> DSI0_LN3_P
- L15 pad 1: /LCM/DSI0_LN2_N -> DSI0_LN2_N
- L15 pad 4: /LCM/DSI0_LN2_P -> DSI0_LN2_P
- L16 pad 1: /LCM/DSI0_LN1_N -> DSI0_LN1_N
- L16 pad 4: /LCM/DSI0_LN1_P -> DSI0_LN1_P
- L17 pad 1: /LCM/DSI0_LN0_N -> DSI0_LN0_N
- L17 pad 4: /LCM/DSI0_LN0_P -> DSI0_LN0_P
- L18 pad 1: /LCM/DSI0_CLK_N -> DSI0_CLK_N
- L18 pad 4: /LCM/DSI0_CLK_P -> DSI0_CLK_P
- L9 pad 1: CSI1_LN3_N -> /HDMI_converter/HDMI_TX0_P
- L9 pad 2: /Cameras_Interface/CSI1_LN3_FFC_N -> Net-(J2-Pad9)
- L9 pad 3: /Cameras_Interface/CSI1_LN3_FFC_P -> Net-(J2-Pad11)
- L9 pad 4: CSI1_LN3_P -> /HDMI_converter/HDMI_TX0_N
- PS1 pad 1: GNDD -> /PoE/SMPS_CTRL
- PS1 pad 4: 5V -> VDD
- Q1 pad 3: CEC_HDMI -> /HDMI_converter/CEC_HDMI
- R1 pad 1: Net-(C1-Pad2) -> (no net)
- R17 pad 1: Net-(J1-Pad11) -> Net-(J1-Pad17)
- R18 pad 1: Net-(J1-Pad13) -> Net-(J1-Pad15)
- R2 pad 1: Net-(C1-Pad2) -> (no net)
- R20 pad 2: CEC_HDMI -> /HDMI_converter/CEC_HDMI
- R21 pad 2: CEC_HDMI -> /HDMI_converter/CEC_HDMI
- R3 pad 1: Net-(C1-Pad2) -> (no net)
- R31 pad 1: 5V0 -> 5V
- R31 pad 2: SCL_HDMI -> /HDMI_converter/SCL_HDMI
- R32 pad 1: 5V0 -> 5V
- R32 pad 2: SDA_HDMI -> /HDMI_converter/SDA_HDMI
- R34 pad 2: DETECT_HDMI -> /HDMI_converter/DETECT_HDMI
- R4 pad 1: Net-(C1-Pad2) -> 3V3
- R6 pad 1: Net-(C4-Pad2) -> /Ethernet_Controller/REG_1V0
- R6 pad 2: Net-(C6-Pad2) -> /Ethernet_Controller/ETH_1V0
- R68 pad 1: /USB-C_Interface /SBU_SW_OE -> SBU_SW_OE
- R7 pad 1: Net-(C5-Pad2) -> Net-(R4-Pad2)
- R7 pad 2: Net-(C6-Pad2) -> GND
- R70 pad 2: 3v075 -> 3V3
- R71 pad 1: /LCM/TP_I2C_SDA -> TP_I2C_SDA
- R71 pad 2: +3V3 -> 3V3
- R72 pad 1: /LCM/TP_I2C_SCL -> TP_I2C_SCL
- R72 pad 2: +3V3 -> 3V3
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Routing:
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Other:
- board text added: "?"

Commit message: Grpuing new parts
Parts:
- added C120: C_100n_0402, antmicro-footprints:0402-cap, F.Cu at (159.8, 97.9)
- added C121: C_100n_0402, antmicro-footprints:0402-cap, F.Cu at (159.5, 104.3)
- added C122: C_10u_0603, antmicro-footprints:0603-cap, F.Cu at (161.1, 103.2)
- added C123: C_4u7_0603, antmicro-footprints:0603-cap, F.Cu at (3.90, 95.3)
- added C124: C_1u_0603, antmicro-footprints:0603-cap, F.Cu at (3.90, 99.9)
- added D20: TPD4E05U06_PASS, antmicro-footprints:TPD4E05U06_PASS, F.Cu at (171.0, 92.5)
- added D21: TPD4E05U06_PASS, antmicro-footprints:TPD4E05U06_PASS, F.Cu at (171.0, 110.0)
- added D22: ESDA25W, antmicro-footprints:SOT-323, F.Cu at (6.80, 107.6)
- added D23: PMEG6002EJ,115, antmicro-footprints:SOD-323F, F.Cu at (4.20, 97.6)
- added IC2: AP22652W6-7, antmicro-footprints:SOT-23-6, F.Cu at (158.5, 101.2)
- added J11: WE_632723300011, sa800u-baseboard-hw-footprints:WE_632723300011, F.Cu at (7.40, 118.1)
- added R100: R_10k_0402, antmicro-footprints:0402-res, F.Cu at (157.5, 104.3)
- added R101: R_20k_0402, antmicro-footprints:0402-res, F.Cu at (158.5, 104.3)
- added R102: R_470R_0402, antmicro-footprints:0402-res, F.Cu at (5.70, 97.7)
- added R103: R_1k_0402, antmicro-footprints:0402-res, F.Cu at (5.70, 99.7)
- added U18: STUSB4500QTR, antmicro-footprints:QFN50P400X400X90-25N, F.Cu at (7.00, 103.4)
- J9: moved to F.Cu
- moved J9 30.0 mm to (173.5, 99.2)
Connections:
- J9 pad 1: (no net) -> SDMMC_DAT2
- J9 pad 2: (no net) -> SDMMC_DAT3
- J9 pad 3: (no net) -> SDMMC_CMD
- J9 pad 4: (no net) -> /Other_Interfaces/SDMCC_VDD
- J9 pad 5: (no net) -> SDMMC_CLK
- J9 pad 6: (no net) -> GND
- J9 pad 7: (no net) -> SDMMC_DAT0
- J9 pad 8: (no net) -> SDMMC_DAT1
- J9 pad 9: Net-(J9-Pad9) -> GND

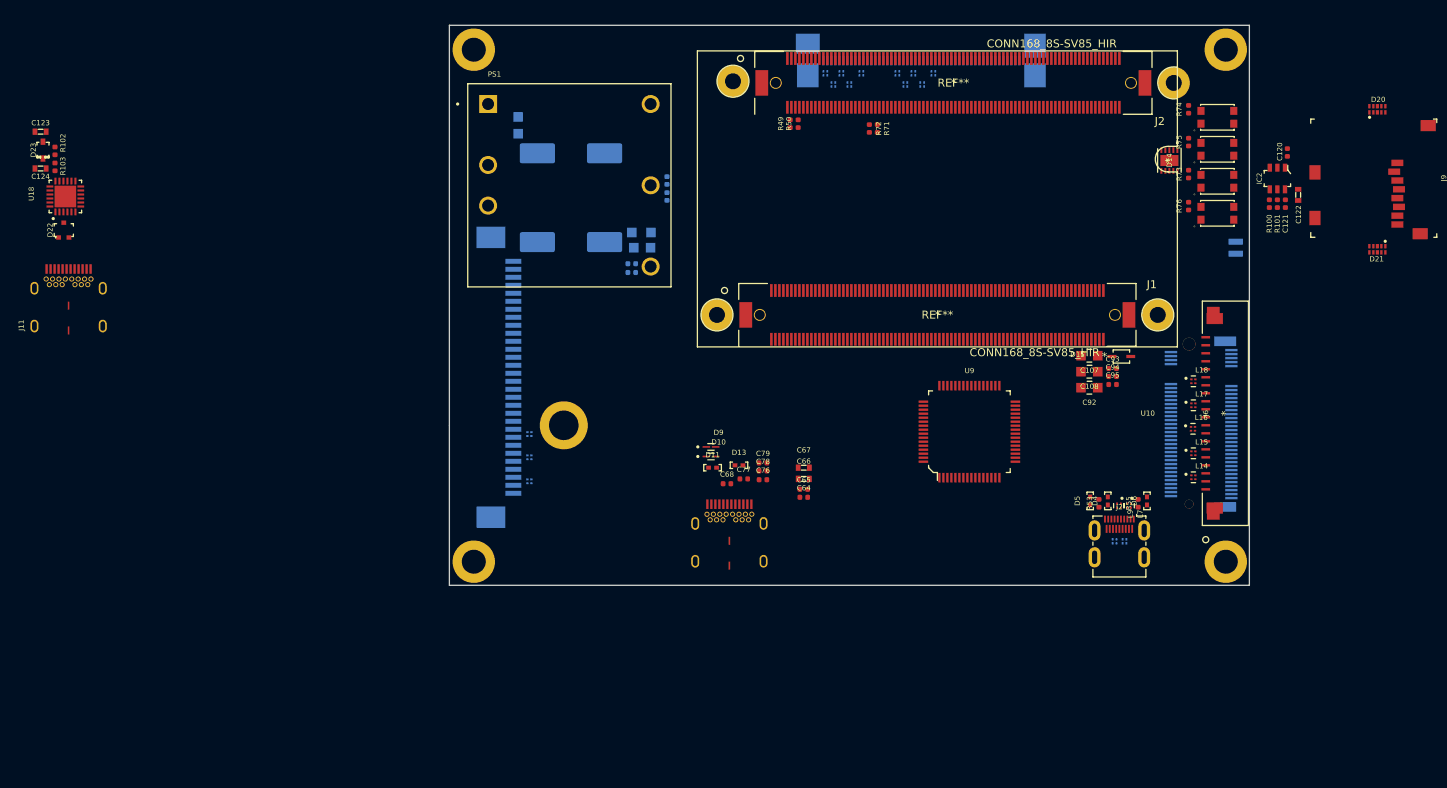
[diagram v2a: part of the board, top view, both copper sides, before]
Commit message: Add USB debug circuitry, loclib
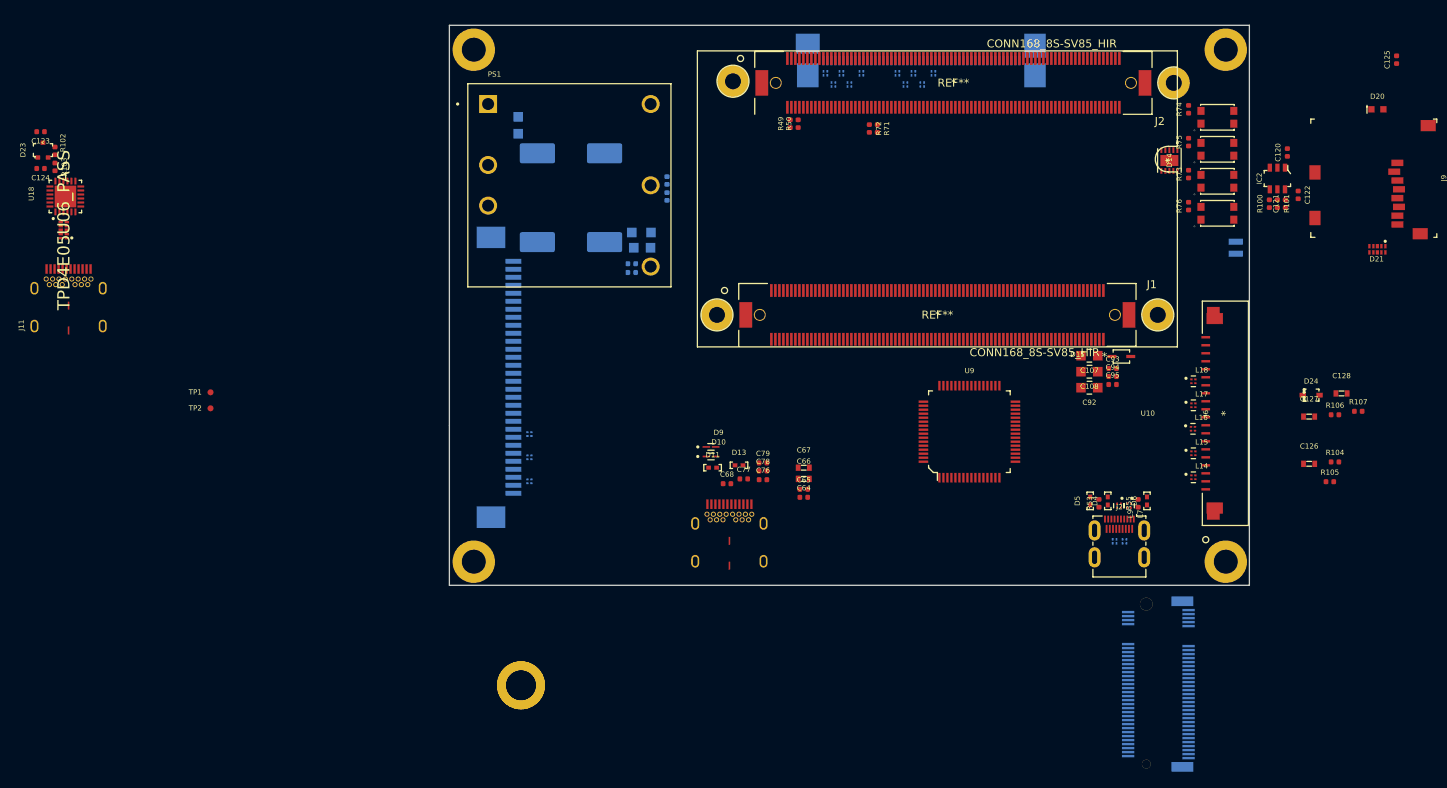
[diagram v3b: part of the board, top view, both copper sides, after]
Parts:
- added C125: C_100n_0402, sa800u-baseboard-hw-footprints:0402-cap, F.Cu at (173.4, 86.3)
- added C126: C_10u_0603, sa800u-baseboard-hw-footprints:0603-cap, F.Cu at (162.5, 136.8)
- added C127: C_4u7_0603, sa800u-baseboard-hw-footprints:0603-cap, F.Cu at (162.5, 130.9)
- added C128: C_1u_0603, sa800u-baseboard-hw-footprints:0603-cap, F.Cu at (166.5, 128.0)
- added D24: PMEG6002EJ,115, sa800u-baseboard-hw-footprints:SOD-323F, F.Cu at (162.7, 128.2)
- added R104: R_10k_0402, sa800u-baseboard-hw-footprints:0402-res, F.Cu at (165.7, 136.6)
- added R105: R_20k_0402, sa800u-baseboard-hw-footprints:0402-res, F.Cu at (165.1, 139.1)
- added R106: R_470R_0402, sa800u-baseboard-hw-footprints:0402-res, F.Cu at (165.7, 130.7)
- added R107: R_1k_0402, sa800u-baseboard-hw-footprints:0402-res, F.Cu at (168.6, 130.2)
- added SP1: 9774040151, sa800u-baseboard-hw-footprints:9774040151, B.Cu at (63.9, 164.4)
- added TP1: TP_SMD_0_75MM, sa800u-baseboard-hw-footprints:Testpoint_smd_0_75mm, F.Cu at (25.1, 127.9)
- added TP2: TP_SMD_0_75MM, sa800u-baseboard-hw-footprints:Testpoint_smd_0_75mm, F.Cu at (25.1, 129.9)
- C1, C110, C121: footprint antmicro-footprints:0402-cap -> sa800u-baseboard-hw-footprints:0402-cap
- C109, C11, C111, C112, C114, C115, C116, C117, C118, C119, C13, C9: footprint antmicro-footprints:0603-cap -> sa800u-baseboard-hw-footprints:0603-cap
- C120: value C_100n_0402 -> C_1u_0402; footprint antmicro-footprints:0402-cap -> sa800u-baseboard-hw-footprints:0402-cap
- C122: value C_10u_0603 -> C_100n_0402; footprint antmicro-footprints:0603-cap -> sa800u-baseboard-hw-footprints:0402-cap
- C123: value C_4u7_0603 -> C_100n_0402; footprint antmicro-footprints:0603-cap -> sa800u-baseboard-hw-footprints:0402-cap
- C124: value C_1u_0603 -> C_100n_0402; footprint antmicro-footprints:0603-cap -> sa800u-baseboard-hw-footprints:0402-cap
- D1, D2: footprint antmicro-footprints:SOT-23-3 -> sa800u-baseboard-hw-footprints:SOT-23-3
- D20: value TPD4E05U06_PASS -> KP-1608CGCK; footprint antmicro-footprints:TPD4E05U06_PASS -> sa800u-baseboard-hw-footprints:LED_0603
- D21: footprint antmicro-footprints:TPD4E05U06_PASS -> sa800u-baseboard-hw-footprints:TPD4E05U06_PASS
- D22: value ESDA25W -> TPD4E05U06_PASS; footprint antmicro-footprints:SOT-323 -> sa800u-baseboard-hw-footprints:TPD4E05U06_PASS
- D23: value PMEG6002EJ,115 -> ESDA25W; footprint antmicro-footprints:SOD-323F -> sa800u-baseboard-hw-footprints:SOT-323
- IC2: footprint antmicro-footprints:SOT-23-6 -> sa800u-baseboard-hw-footprints:SOT-23-6
- J1: footprint antmicro-footprints:5-2337992-8 -> sa800u-baseboard-hw-footprints:5-2337992-8
- L29, L30, L31, L32: footprint antmicro-footprints:Coilcraft-XEL4030 -> sa800u-baseboard-hw-footprints:Coilcraft-XEL4030
- MP1, MP2, MP3, MP4: footprint antmicro-footprints:9774030243R -> sa800u-baseboard-hw-footprints:9774030243R
- Q6: footprint antmicro-footprints:IRF7416TRPBF -> sa800u-baseboard-hw-footprints:IRF7416TRPBF
- R1, R10, R100, R2, R3, R4, R7, R9, R91, R92, R93, R97, R98, R99: footprint antmicro-footprints:0402-res -> sa800u-baseboard-hw-footprints:0402-res
- R101: value R_20k_0402 -> R_10k_0402; footprint antmicro-footprints:0402-res -> sa800u-baseboard-hw-footprints:0402-res
- R102: value R_470R_0402 -> R_220R_0402; footprint antmicro-footprints:0402-res -> sa800u-baseboard-hw-footprints:0402-res
- R103: value R_1k_0402 -> R_10k_0402; footprint antmicro-footprints:0402-res -> sa800u-baseboard-hw-footprints:0402-res
- R8: footprint antmicro-footprints:0402 -> sa800u-baseboard-hw-footprints:0402
- U16: footprint antmicro-footprints:SOT-23-5 -> sa800u-baseboard-hw-footprints:SOT-23-5
- U18: footprint antmicro-footprints:QFN50P400X400X90-25N -> sa800u-baseboard-hw-footprints:QFN50P400X400X90-25N
- U2: footprint antmicro-footprints:LT9611 -> sa800u-baseboard-hw-footprints:LT9611
- moved U12 32.9 mm to (63.6, 175.5)
- turned C120 to 90 degrees
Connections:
- C120 pad 1: GND -> 3V3
- C120 pad 2: 3V3 -> GND
- C121 pad 1: GND -> 3V3
- C121 pad 2: /Other_Interfaces/SDMCC_VDD -> GND
- C122 pad 1: /Other_Interfaces/SDMCC_VDD -> /M2/C_PCIE0_TX0_P
- C122 pad 2: GND -> PCIE0_TX_P
- C123 pad 1: /USB-PD/PD_VBUS -> /M2/C_PCIE0_TX0_N
- C123 pad 2: GND -> PCIE0_TX_N
- C124 pad 1: Net-(C124-Pad1) -> GND
- C124 pad 2: GND -> 3V3
- D20 pad 1: SDMMC_DAT3 -> Net-(D20-Pad1)
- D20 pad 2: SDMMC_DAT2 -> Net-(D20-Pad2)
- D21 pad 1: SDMMC_DAT1 -> SD_DATA3
- D21 pad 2: SDMMC_DAT0 -> SD_DATA2
- D21 pad 4: SDMMC_CLK -> SD_DET
- D21 pad 5: SDMMC_CMD -> Net-(D21-Pad5)
- D22 pad 1: Net-(D22-Pad1) -> SD_DATA1
- D22 pad 2: Net-(D22-Pad2) -> SD_DATA0
- J11 pad A5: Net-(D22-Pad1) -> Net-(D23-Pad1)
- J11 pad B5: Net-(D22-Pad2) -> Net-(D23-Pad2)
- J9 pad 1: SDMMC_DAT2 -> SD_DATA2
- J9 pad 2: SDMMC_DAT3 -> SD_DATA3
- J9 pad 3: SDMMC_CMD -> SD_CMD
- J9 pad 5: SDMMC_CLK -> SD_CLK
- J9 pad 7: SDMMC_DAT0 -> SD_DATA0
- J9 pad 8: SDMMC_DAT1 -> SD_DATA1
- R100 pad 2: /Other_Interfaces/SDMCC_VDD_FAULT# -> PCIE0_WAKE_N
- R101 pad 1: /Other_Interfaces/SDMCC_VDD_ILIM -> 3V3
- R101 pad 2: GND -> PCIE0_CLKREQ_N
- R102 pad 1: /USB-PD/PD_VBUS -> 3V3
- R102 pad 2: Net-(C124-Pad1) -> Net-(D20-Pad1)
- R103 pad 1: Net-(C124-Pad1) -> 3V3
- R103 pad 2: Net-(R103-Pad2) -> M2_ALERT
- U10 pad 1_1: (no net) -> PCIE0_RST_N
- U10 pad 1_11: (no net) -> PCIE0_TX_P
- U10 pad 1_15: (no net) -> PCIE0_REFCLK_P
- U10 pad 1_17: (no net) -> PCIE0_REFCLK_N
- U10 pad 1_21: (no net) -> PCIE0_RX_P
- U10 pad 1_23: (no net) -> PCIE0_RX_N
- U10 pad 1_3: (no net) -> PCIE0_WAKE_N
- U10 pad 1_45: (no net) -> SD_CLK
- U10 pad 1_47: (no net) -> SD_CMD
- U10 pad 1_49: (no net) -> SD_DET
- U10 pad 1_5: (no net) -> PCIE0_CLKREQ_N
- U10 pad 1_51: (no net) -> SD_DATA0
- U10 pad 1_53: (no net) -> SD_DATA1
- U10 pad 1_55: (no net) -> SD_DATA3
- U10 pad 1_57: (no net) -> SD_DATA2
- U10 pad 1_9: (no net) -> PCIE0_TX_N
- U12 pad 1: (no net) -> GND
- U12 pad 10: (no net) -> Net-(D20-Pad2)
- U12 pad 12: (no net) -> 3V3
- U12 pad 14: (no net) -> 3V3
- U12 pad 15: (no net) -> GND
- U12 pad 16: (no net) -> 3V3
- U12 pad 18: (no net) -> 3V3
- U12 pad 2: (no net) -> 3V3
- U12 pad 21: (no net) -> GND
- U12 pad 27: (no net) -> GND
- U12 pad 3: (no net) -> GND
- U12 pad 33: (no net) -> GND
- U12 pad 39: (no net) -> GND
- U12 pad 4: (no net) -> 3V3
- U12 pad 40: (no net) -> Net-(TP2-Pad1)
- U12 pad 41: (no net) -> PCIE0_RX_N
- U12 pad 42: (no net) -> Net-(TP1-Pad1)
- U12 pad 43: (no net) -> PCIE0_RX_P
- U12 pad 44: (no net) -> M2_ALERT
- U12 pad 45: (no net) -> GND
- U12 pad 47: (no net) -> /M2/C_PCIE0_TX0_N
- U12 pad 49: (no net) -> /M2/C_PCIE0_TX0_P
- U12 pad 50: (no net) -> PCIE0_CLKREQ_N
- U12 pad 51: (no net) -> GND
- U12 pad 52: (no net) -> PCIE0_WAKE_N
- U12 pad 53: (no net) -> PCIE0_REFCLK_N
- U12 pad 54: (no net) -> PCIE0_RST_N
- U12 pad 55: (no net) -> PCIE0_REFCLK_P
- U12 pad 57: (no net) -> GND
- U12 pad 70: (no net) -> 3V3
- U12 pad 71: (no net) -> GND
- U12 pad 72: (no net) -> 3V3
- U12 pad 73: (no net) -> GND
- U12 pad 74: (no net) -> 3V3
- U12 pad 75: (no net) -> GND
- U12 pad 9: (no net) -> GND
- U12 pad SH1: (no net) -> GND
- U12 pad SH2: (no net) -> GND
- U18 pad 1: Net-(D22-Pad1) -> Net-(D23-Pad1)
- U18 pad 18: Net-(R103-Pad2) -> Net-(R107-Pad2)
- U18 pad 2: Net-(D22-Pad1) -> Net-(D23-Pad1)
- U18 pad 4: Net-(D22-Pad2) -> Net-(D23-Pad2)
- U18 pad 5: Net-(D22-Pad2) -> Net-(D23-Pad2)
